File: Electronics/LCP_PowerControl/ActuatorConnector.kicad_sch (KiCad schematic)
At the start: 2 parts, among them J17 Conn_01x02, J18 Conn_01x04

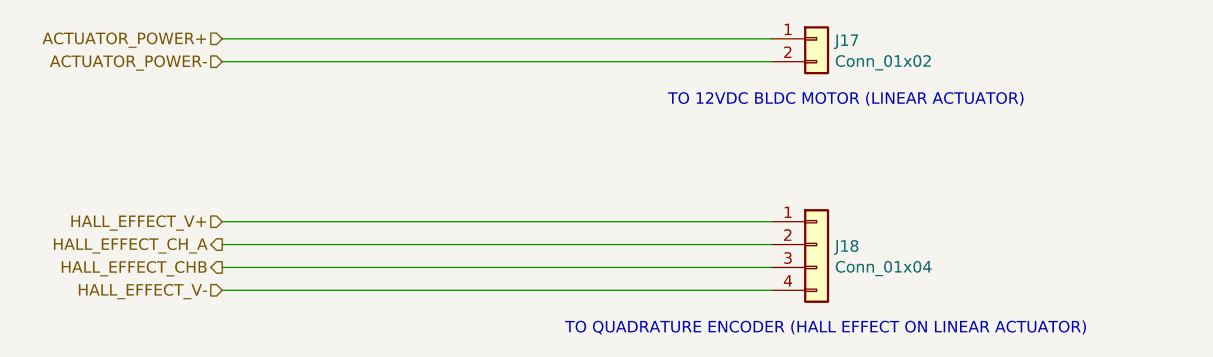
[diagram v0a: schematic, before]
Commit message: Updated Connectors
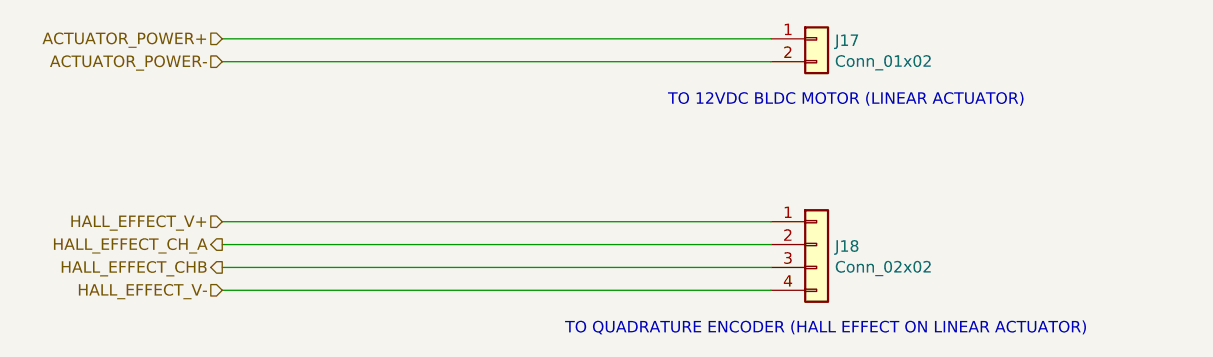
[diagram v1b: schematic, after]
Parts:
- J18: value Conn_01x04 -> Conn_02x02
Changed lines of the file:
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@@
   (paper "A4")
   (title_block
-    (date "2020-06-17")
-    (rev "R0.1")
+    (date "2024-07-22")
+    (rev "1.3")
     (comment 1 "Design by: Matt Casari")
+    (comment 2 "Updated by Joseph Kurina")
   )
   (wire (pts (xy 123.19 105.41) (xy 184.15 105.41))
@@
       (effects (font (size 1.27 1.27)) (justify left))
     )
-    (property "Value" "Conn_01x04" (at 191.262 105.3846 0)
+    (property "Value" "Conn_02x02" (at 191.262 105.3846 0)
       (effects (font (size 1.27 1.27)) (justify left))
     )
